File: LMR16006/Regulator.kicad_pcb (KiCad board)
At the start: 2 copper layers, 10.2 x 12.7 mm, 10 parts, among them J1 Conn_01x04, U1 LMR16006XDDCR

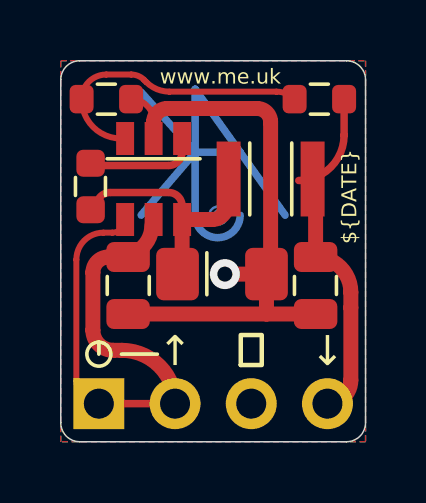
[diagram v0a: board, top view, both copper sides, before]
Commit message: Put back regulator
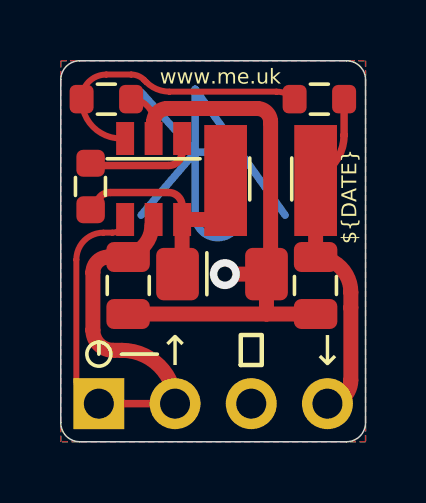
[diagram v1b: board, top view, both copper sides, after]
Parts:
- J1: footprint RevK:PinHeader_1x04_P2.54mm_Right -> RevK:JLC-PinHeader_1x04_P2.54mm_Right
- L1: footprint RevK:L_1210_ -> RevK:L_4x4_
- R1: value 10M 1% -> 100k 1%
- R2: value 1.8M 1% -> 30k 1%
- U1: footprint RevK:SOT-23-Thin-6-Reg2 -> RevK:SOT-23-Thin-6-Reg

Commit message: Tweaks for production
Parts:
- turned U1 to 0 degrees
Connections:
- U1 pad 1: Net-(J1-Pad1) -> unconnected-(U1-Pad1)
- U1 pad 2: Net-(J1-Pad1) -> GND
- U1 pad 3: GND -> Net-(R1-Pad2)
- U1 pad 4: Net-(J1-Pad4) -> Net-(J1-Pad1)
- U1 pad 5: Net-(R1-Pad2) -> Net-(J1-Pad1)
